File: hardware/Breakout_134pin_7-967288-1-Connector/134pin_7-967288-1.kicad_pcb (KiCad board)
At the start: 2 copper layers, 139.7 x 73.7 mm, 40 parts, among them J1 Conn_01x03, J10 Conn_01x06, J11 Conn_01x06, J12 Conn_01x03, J13 Conn_01x03, J14 Conn_01x03, J15 Conn_01x13, J16 Conn_01x13, J17 Conn_01x13, J18 Conn_01x13, J19 Conn_01x13, J2 Conn_01x03, J20 Conn_01x13, J21 Conn_01x13, J22 Conn_01x13, J23 Conn_01x10, J24 Conn_01x10, J25 Conn_01x10, J26 Conn_01x10, J27 Conn_01x03, J28 Conn_01x03, J29 Conn_01x03, J3 Conn_01x03, J30 Conn_01x10, J31 Conn_01x10, J32 Conn_01x10, J33 Conn_01x10, J34 Conn_01x03, J35 Conn_01x03, J36 Conn_01x03, J37 Conn_01x01, J4 Conn_01x06, J5 Conn_01x06, J6 Conn_01x06, J7 Conn_01x06, J8 Conn_01x06, J9 Conn_01x06, P1 134pin_7-967288-1_KC5

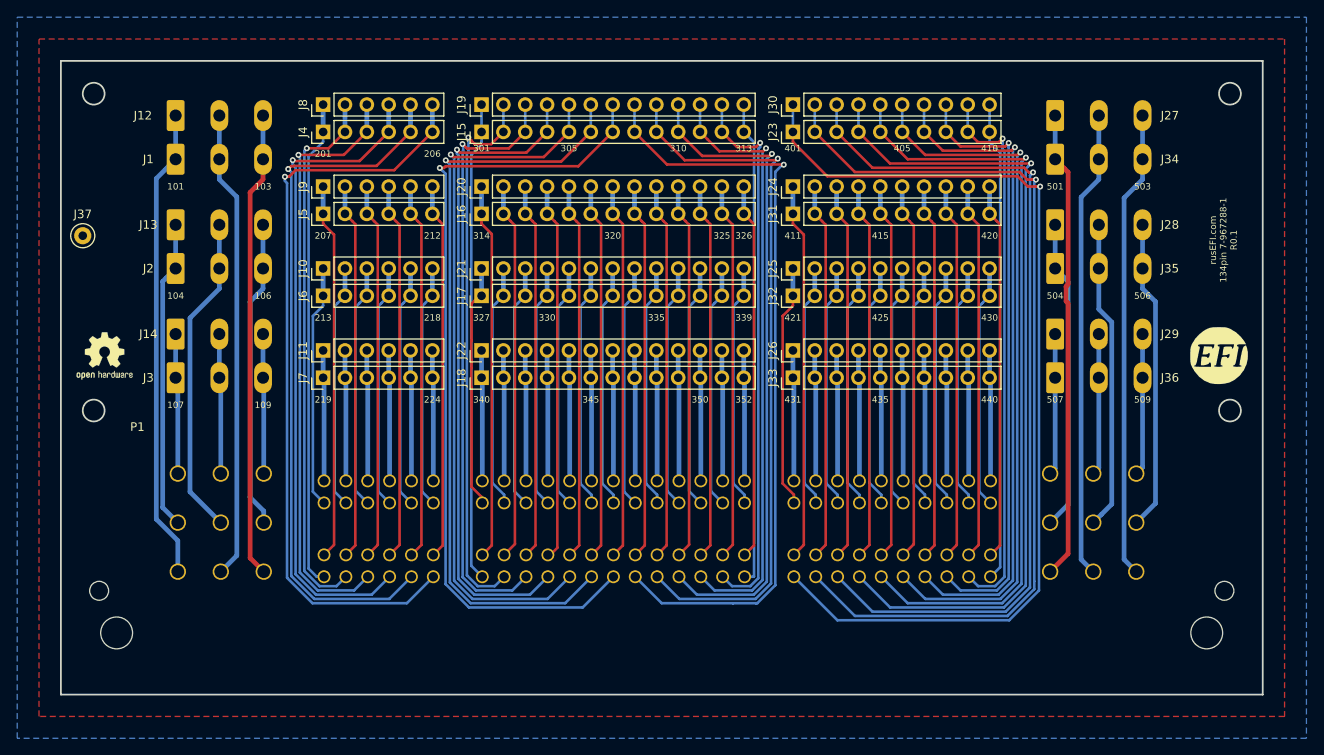
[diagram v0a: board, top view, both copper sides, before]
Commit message: Thickened the traces on the outer pads.
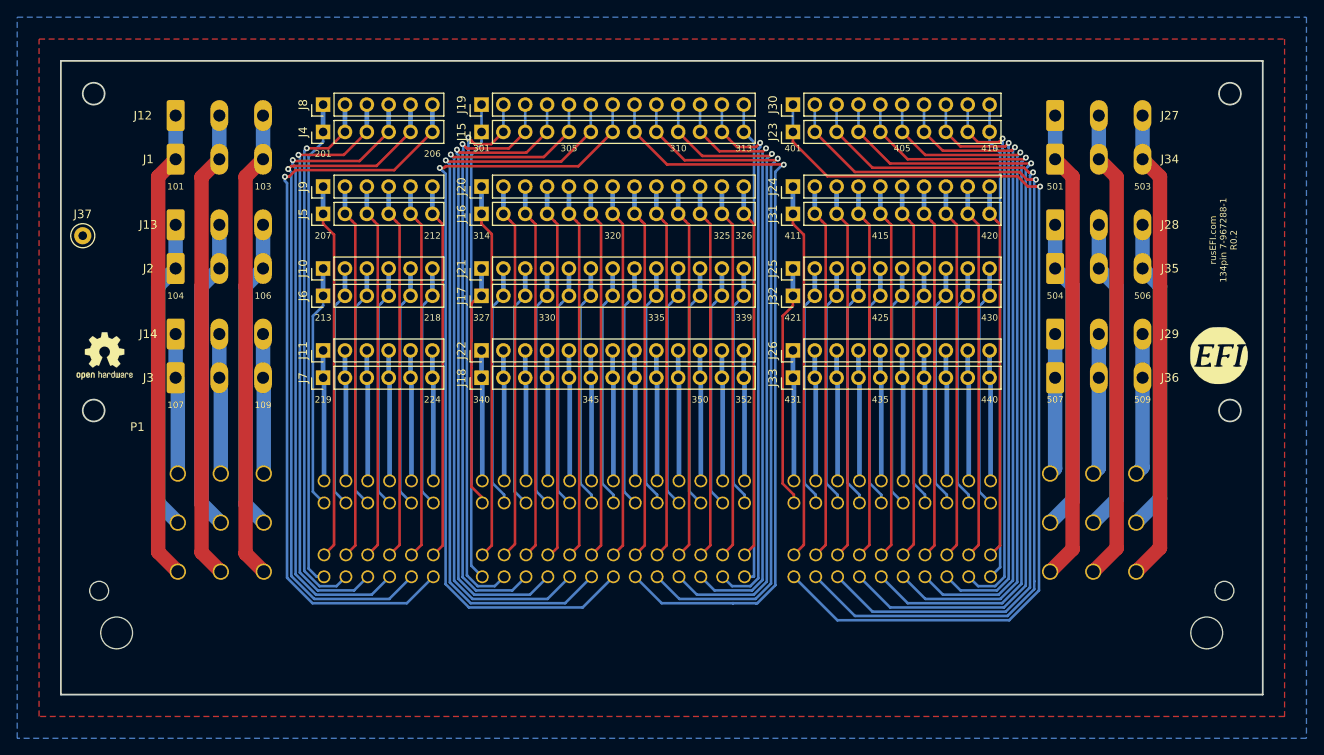
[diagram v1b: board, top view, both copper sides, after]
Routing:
- net Net-(J13-Pad2): track 37.5 -> 36.4 mm
- net Net-(J27-Pad2): track 54.5 -> 55.0 mm
- net /503: track 54.5 -> 55.0 mm
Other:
- board text added: "rusEFI.com 134pin 7-967288-1 R0.2"
- board text removed: "rusEFI.com 134pin 7-967288-1 R0.1"
